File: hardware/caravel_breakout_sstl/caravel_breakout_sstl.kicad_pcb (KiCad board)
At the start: 2 copper layers, 25.4 x 25.4 mm, 20 parts, among them J1 Conn_01x14_Female, J2 Conn_01x14_Female, J3 Conn_01x14_Female, J4 Conn_01x14_Female, T1 Logo, T2 Logo, U1 Caravel

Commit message: Finish draft of Layout
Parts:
- removed H1, H2, H3, H4: Positioning Holes, MountingHole:MountingHole_2.2mm_M2_ISO7380_Pad
- added C10: 10uf, Capacitor_SMD:C_0805_2012Metric, F.Cu at (119.2, 77.9)
- added C11: 10uf, Capacitor_SMD:C_0805_2012Metric, F.Cu at (122.6, 78.2)
- added C12: 0.1uf, Capacitor_SMD:C_0402_1005Metric, F.Cu at (122.1, 81.5)
- added C13: 0.1uf, Capacitor_SMD:C_0402_1005Metric, F.Cu at (137.0, 105.4)
- added C14: 0.1uf, Capacitor_SMD:C_0402_1005Metric, F.Cu at (138.3, 97.9)
- added C15: 0.1uf, Capacitor_SMD:C_0402_1005Metric, F.Cu at (125.3, 105.5)
- added C16: 0.1uf, Capacitor_SMD:C_0402_1005Metric, F.Cu at (126.7, 98.0)
- added JP1: Jumper_3_Open, Connector_PinHeader_2.54mm:PinHeader_1x03_P2.54mm_Vertical, F.Cu at (124.3, 84.3)
- added R1: 80.6ohm, Resistor_SMD:R_0402_1005Metric, F.Cu at (124.8, 89.2)
- added R2: 80.6ohm, Resistor_SMD:R_0402_1005Metric, F.Cu at (124.8, 90.2)
- added R3: 80.6ohm, Resistor_SMD:R_0402_1005Metric, F.Cu at (124.8, 91.9)
- added R4: 80.6ohm, Resistor_SMD:R_0402_1005Metric, F.Cu at (124.8, 92.9)
- added TP1: TestPoint_2Pole, TestPoint:TestPoint_2Pads_Pitch2.54mm_Drill0.8mm, F.Cu at (127.0, 89.7)
- added TP2: TestPoint_2Pole, TestPoint:TestPoint_2Pads_Pitch2.54mm_Drill0.8mm, F.Cu at (127.0, 92.3)
- added U2: LTC1844ES5-1.5, Package_TO_SOT_SMD:TSOT-23-5, F.Cu at (119.5, 80.7)
- added U3: SN74AVC4T245PW, custom_footprints:Texas_R-PDSO-G16, F.Cu at (131.1, 102.7)
- added U4: SN74AVC4T245PW, custom_footprints:Texas_R-PDSO-G16, F.Cu at (142.8, 102.7)
- J1, J3, J4: value Conn_01x14_Female -> Conn_02x07_Top_Bottom; footprint Connector_PinHeader_1.27mm:PinHeader_2x14_P1.27mm_Vertical -> Connector_PinSocket_2.54mm:PinSocket_2x07_P2.54mm_Vertical
- J2: value Conn_01x14_Female -> Conn_Coaxial; footprint Connector_PinHeader_1.27mm:PinHeader_2x14_P1.27mm_Vertical -> Connector_Coaxial:SMA_Amphenol_132134-16_Vertical
- moved J1 18.4 mm to (124.8, 108.3), turned to 90 degrees
- moved T1 14.6 mm to (120.1, 106.8)
- moved C7 8.49 mm to (141.2, 93.7), turned to 180 degrees
- moved C3 7.17 mm to (134.1, 94.6), turned to 0 degrees
- moved C1 4.16 mm to (129.7, 95.1), turned to 90 degrees
- moved T2 3.75 mm to (129.7, 83.0)
- moved C5 2.74 mm to (128.7, 95.1), turned to 90 degrees
- moved J4 2.54 mm to (146.8, 81.9)
- moved J3 0.74 mm to (125.4, 78.0)
- moved J2 0.42 mm to (121.6, 97.7), turned to 0 degrees
- moved C2 0.07 mm to (127.2, 85.2)
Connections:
- C3 pad 1: GND -> vdda2
- C3 pad 2: vdda2 -> GND
- J1 pad 1: mprj_io[37] -> vin_3v3
- J1 pad 10: GND -> prbs_clk_1_vin
- J1 pad 12: vccd -> prbs_clk_2_vin
- J1 pad 14: vddio -> ~{prsb_rst_vin}
- J1 pad 2: mprj_io[37] -> GND
- J1 pad 3: mprj_io[36] -> alt_vdd_1v5
- J1 pad 4: mprj_io[36] -> cfg_clk_vin
- J1 pad 5: mprj_io[35] -> cfg_vin
- J1 pad 6: mprj_io[35] -> cfg_din_vin
- J1 pad 7: mprj_io[34] -> GND
- J1 pad 8: mprj_io[34] -> prbs_clk_0_vin
- J2 pad 1: mprj_io[27] -> Net-(J2-Pad1)
- J2 pad 2: mprj_io[27] -> GND
- J3 pad 1: mprj_io[13] -> unconnected-(J3-Pad1)
- J3 pad 10: mprj_io[9] -> mprj_io[2]_SDI
- J3 pad 11: mprj_io[8] -> unconnected-(J3-Pad11)
- J3 pad 12: mprj_io[8] -> mprj_io[1]_SDO
- J3 pad 13: mprj_io[7] -> unconnected-(J3-Pad13)
- J3 pad 14: mprj_io[7] -> mprj_io[0]
- J3 pad 2: mprj_io[13] -> mprj_io[6]_ser_tx
- J3 pad 3: mprj_io[12] -> unconnected-(J3-Pad3)
- J3 pad 4: mprj_io[12] -> mprj_io[5]_ser_rx
- J3 pad 5: mprj_io[11] -> unconnected-(J3-Pad5)
- J3 pad 6: mprj_io[11] -> mprj_io[4]_SCK
- J3 pad 7: mprj_io[10] -> unconnected-(J3-Pad7)
- J3 pad 8: mprj_io[10] -> mprj_io[3]_CSB
- J3 pad 9: mprj_io[9] -> unconnected-(J3-Pad9)
- J4 pad 10: gpio -> vccd
- J4 pad 11: Caravel_D1 -> vdda2
- J4 pad 12: Caravel_D1 -> vddio
- J4 pad 13: Caravel_D0 -> ~{RST}
- J4 pad 14: Caravel_D0 -> vccd2
- J4 pad 2: vccd1 -> vdda1
- J4 pad 3: vdda1 -> gpio
- J4 pad 4: vdda1 -> vdda
- J4 pad 5: vdda -> Caravel_D0
- J4 pad 6: vdda -> Caravel_D1
- J4 pad 7: Caravel_SCK -> Caravel_CSB
- J4 pad 9: gpio -> xclk
- U1 pad 1: unconnected-(U1-Pad1) -> GND
- U1 pad 11: mprj_io[32] -> unconnected-(U1-Pad11)
- U1 pad 12: mprj_io[33] -> unconnected-(U1-Pad12)
- U1 pad 13: mprj_io[34] -> unconnected-(U1-Pad13)
- U1 pad 14: mprj_io[35] -> unconnected-(U1-Pad14)
- U1 pad 15: mprj_io[36] -> unconnected-(U1-Pad15)
- U1 pad 16: mprj_io[37] -> unconnected-(U1-Pad16)
- U1 pad 2: mprj_io[25] -> cfg_din
- U1 pad 3: mprj_io[26] -> cfg_clk
- U1 pad 4: mprj_io[27] -> prbs_clk_0
- U1 pad 41: mprj_io[7] -> unconnected-(U1-Pad41)
- U1 pad 42: mprj_io[8] -> unconnected-(U1-Pad42)
- U1 pad 43: mprj_io[9] -> unconnected-(U1-Pad43)
- U1 pad 44: mprj_io[10] -> unconnected-(U1-Pad44)
- U1 pad 45: mprj_io[11] -> unconnected-(U1-Pad45)
- U1 pad 46: mprj_io[12] -> unconnected-(U1-Pad46)
- U1 pad 48: mprj_io[13] -> unconnected-(U1-Pad48)
- U1 pad 5: mprj_io[28] -> prbs_clk_1
- U1 pad 50: mprj_io[14] -> unconnected-(U1-Pad50)
- U1 pad 51: mprj_io[15] -> unconnected-(U1-Pad51)
- U1 pad 53: mprj_io[16] -> unconnected-(U1-Pad53)
- U1 pad 54: mprj_io[17] -> GND
- U1 pad 55: mprj_io[18] -> analog_vdd
- U1 pad 57: mprj_io[19] -> analog_vdd
- U1 pad 58: mprj_io[20] -> GND
- U1 pad 59: mprj_io[21] -> unconnected-(U1-Pad59)
- U1 pad 6: mprj_io[29] -> prbs_clk_2
- U1 pad 60: mprj_io[22] -> tx_dq
- U1 pad 61: mprj_io[23] -> ~{tx_dq}
- U1 pad 62: mprj_io[24] -> Net-(J2-Pad1)
- U1 pad 7: mprj_io[30] -> ~{prbs_rst}
- U1 pad 8: mprj_io[31] -> unconnected-(U1-Pad8)
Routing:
- net analog_vdd: track 0.00 -> 47.9 mm, vias 0 -> 2
- net vin_3v3: track 0.00 -> 34.1 mm, vias 0 -> 2
- net alt_vdd_1v5: track 0.00 -> 28.9 mm
- net cfg_vin: track 0.00 -> 23.1 mm, vias 0 -> 2
- net ~{prbs_rst}: track 0.00 -> 17.0 mm
- net prbs_clk_2: track 0.00 -> 16.6 mm
- net prbs_clk_1: track 0.00 -> 15.5 mm
- net GND: track 68.7 -> 53.8 mm, vias 11 -> 8
- net prbs_clk_0: track 0.00 -> 14.5 mm
- net mprj_io[27]: track 13.8 -> 0.00 mm
- net prbs_clk_0_vin: track 0.00 -> 13.5 mm
- net mprj_io[26]: track 13.5 -> 0.00 mm
- net mprj_io[13]: track 13.1 -> 0.00 mm
- net prbs_clk_2_vin: track 0.00 -> 12.4 mm, vias 0 -> 2
- net mprj_io[28]: track 11.8 -> 0.00 mm
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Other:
- board size 25.4 x 25.4 mm -> 31.3 x 36.5 mm
- board text removed: "29"
- board text removed: "43"

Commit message: Add logos to back
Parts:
- added G***: LOGO, custom_footprints:cse_logo_2, B.Cu at (132.9, 104.5)
- added G***: LOGO, custom_footprints:uw_logo, B.Cu at (134.3, 88.3)

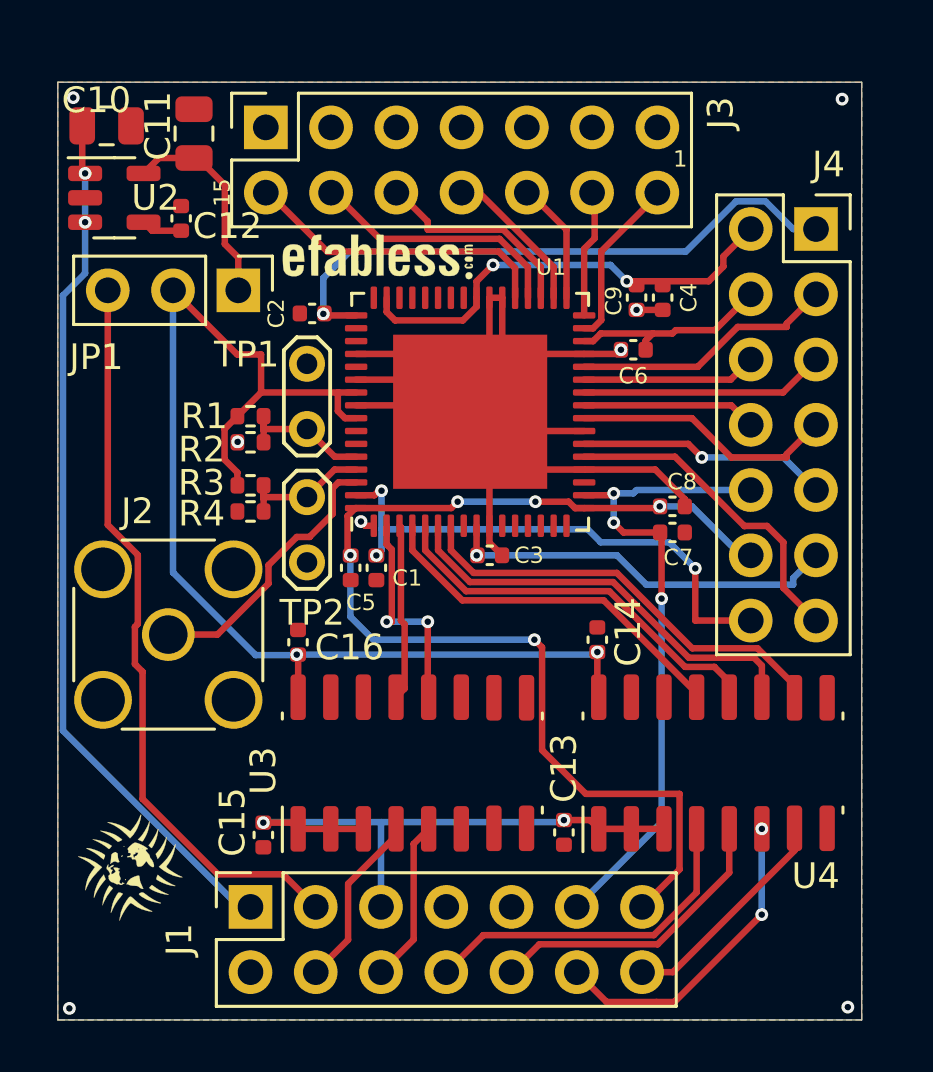
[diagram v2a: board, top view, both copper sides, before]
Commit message: Minor updates to improve routing
Ground all unused pins
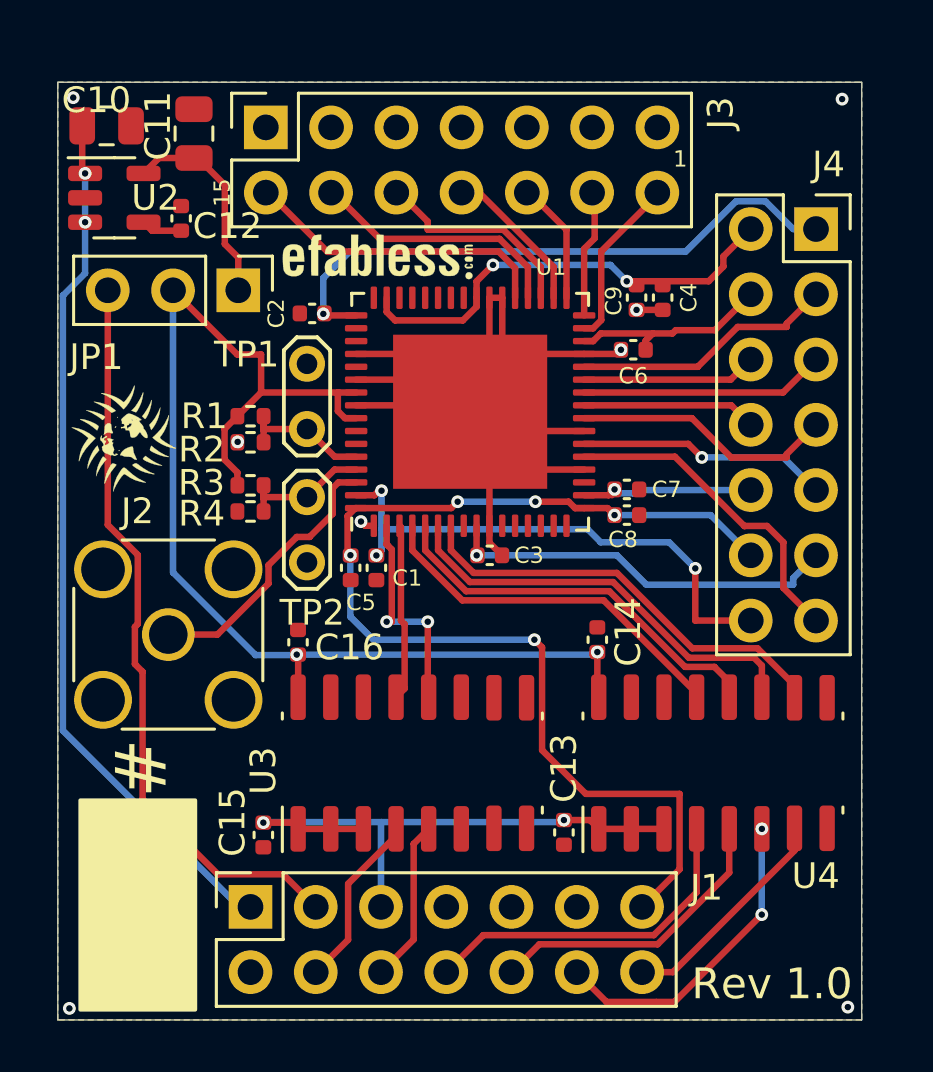
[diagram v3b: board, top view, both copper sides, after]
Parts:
- moved T1 16.7 mm to (119.8, 90.0)
- moved C7 2.44 mm to (139.4, 92.0)
- moved C8 1.81 mm to (139.4, 93.0)
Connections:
- J1 pad 11: vccd -> GND
- J3 pad 1: unconnected-(J3-Pad1) -> GND
- J3 pad 11: unconnected-(J3-Pad11) -> GND
- J3 pad 13: unconnected-(J3-Pad13) -> GND
- J3 pad 3: unconnected-(J3-Pad3) -> GND
- J3 pad 5: unconnected-(J3-Pad5) -> GND
- J3 pad 7: unconnected-(J3-Pad7) -> GND
- J3 pad 9: unconnected-(J3-Pad9) -> GND
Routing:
- net vccd: track 25.6 -> 6.77 mm, vias 3 -> 1
- net GND: track 53.8 -> 49.0 mm
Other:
- board text added: "#"
- board text added: "Rev 1.0"
